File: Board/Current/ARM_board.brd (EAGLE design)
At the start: 101.6 x 81.3 mm, 178 parts, among them IC3 STM32F437VI, IC4 LM358DT, J1 USART/I2C, J10 ANALOG, J11 DGND, J12 DPWR, J13 DIGITAL, J14 SGND, J15 SPWR, J16 SERVO, J2 I2C2/USART3, J3 USART2, J5 SPI, J6 Bluesmirf, J7 SWD, J8 AGND, J9 APWR, Q1 STL4P2UH7, Q2 2STR1230, Q3 STL4P2UH7, SW1 SW, U1 LSM330, U10 BAV99, U11 BAV99, U12 USBLC6-2, U13 USBLC6-2, U14 STMPS2171MTR, U15 MC74HC164, U3 NC7SZU04, U4 L6206Q, U5 L6206Q, U6 SI7617, U7 SI7617, U8 SI7617, U9 SI7617, Y2 8MHz

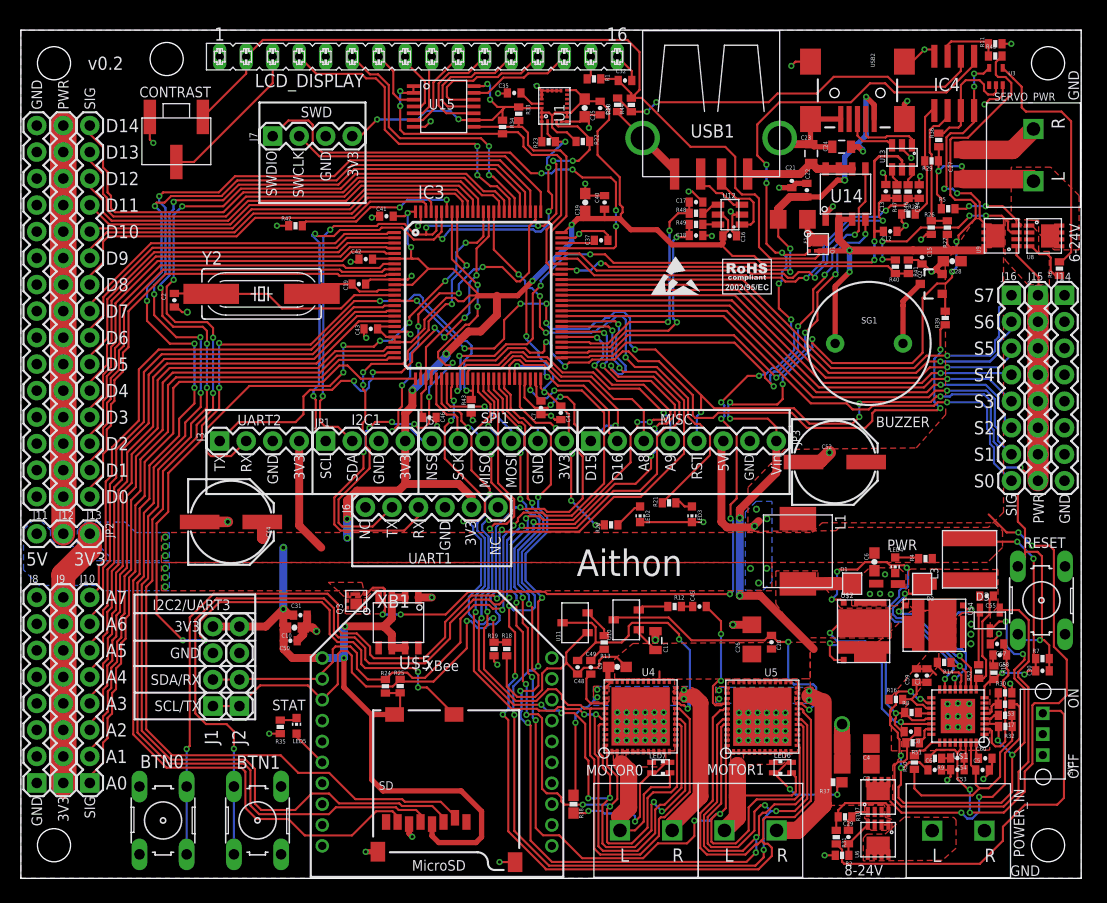
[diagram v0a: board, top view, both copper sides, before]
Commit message: Went through the size of all the passives.
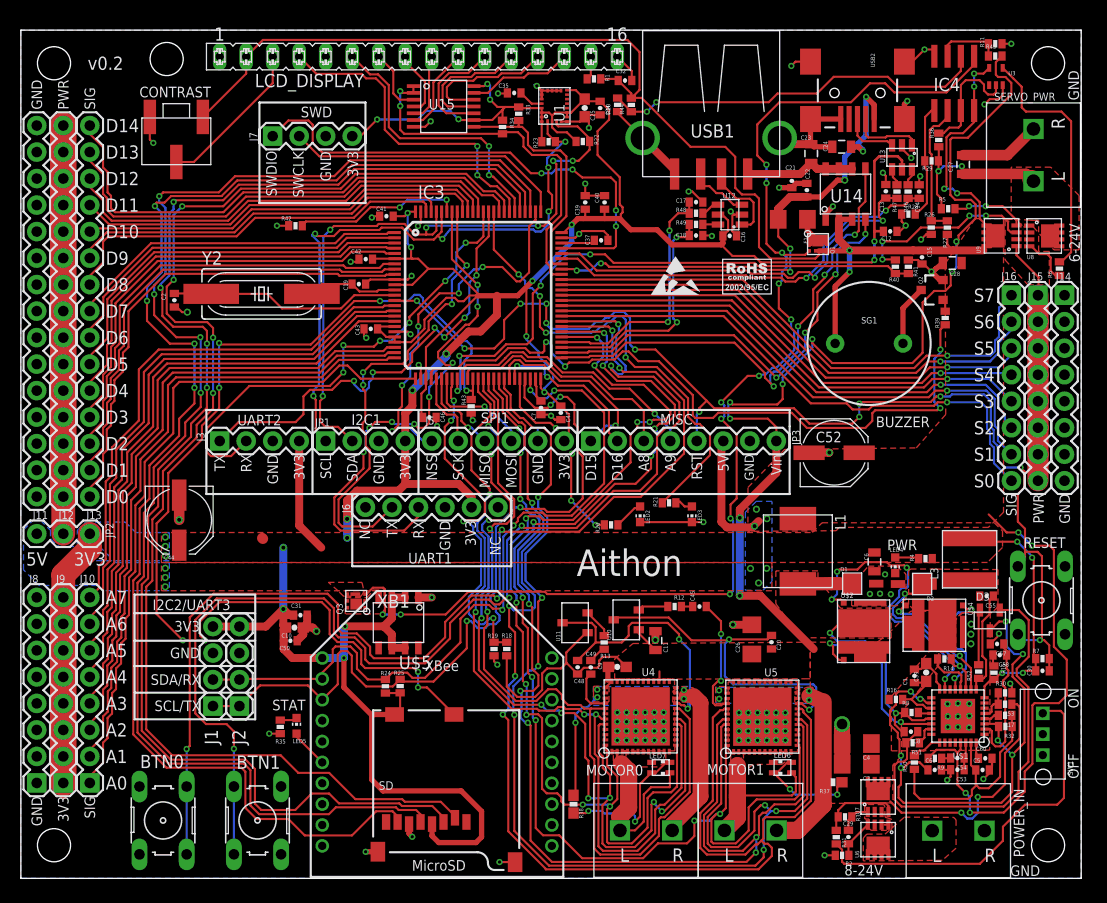
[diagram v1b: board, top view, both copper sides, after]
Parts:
- C27: value 22u -> 33u; device SparkFun:1206 -> SparkFun:0805
- C28, C6: device SparkFun:0603-CAP -> SparkFun:0805
- C39: device SparkFun:0603-CAP -> SparkFun:0402-CAP
- C44, C52: device SparkFun:PANASONIC_E -> SparkFun:PANASONIC_D
- C59: device SparkFun:0402-CAP -> SparkFun:0603-CAP
- moved C44 4.96 mm to (15.2, 34.3), turned to 270 degrees
- moved C1 1.19 mm to (85.6, 19.4)
- moved C59 0.97 mm to (86.7, 19.7)
- moved C52 0.89 mm to (77.9, 40.8)
- moved Q2 0.58 mm to (87.4, 56.4)
- moved R14 0.32 mm to (88.5, 21.0)
- moved C28 0.18 mm to (89.2, 59.0)
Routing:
- net N$39: track 28.5 -> 33.1 mm
- net GND: track 150.6 -> 152.5 mm
- net +3V3: track 373.3 -> 371.9 mm
- net N$15: track 22.1 -> 22.8 mm
- net N$79: track 5.92 -> 6.58 mm
- net ANALOG9: track 26.2 -> 25.7 mm
- net N$28: track 6.39 -> 5.85 mm

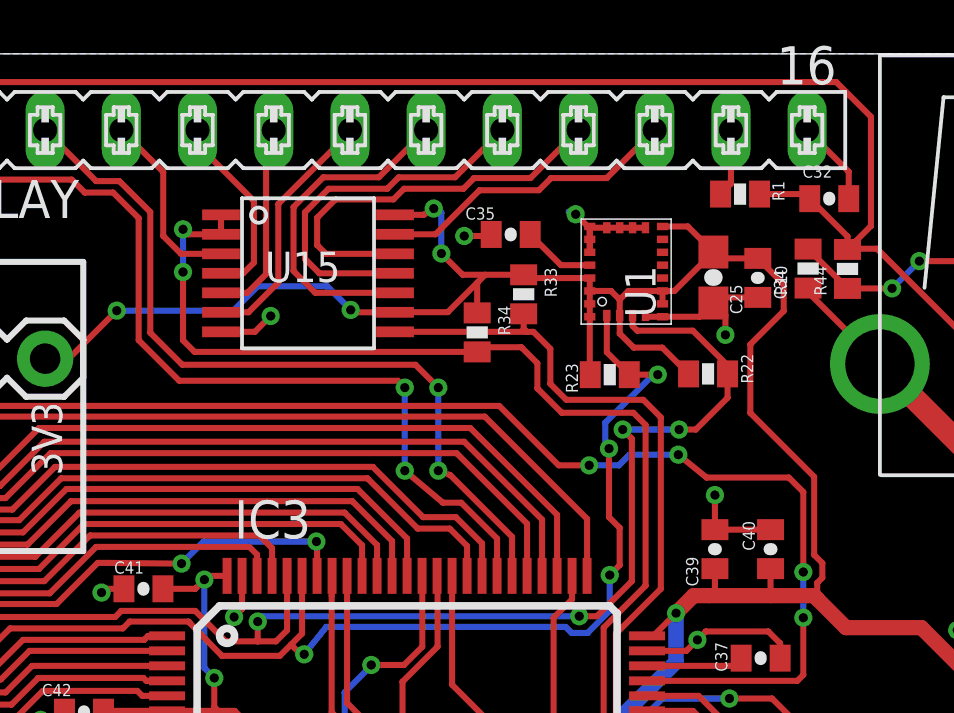
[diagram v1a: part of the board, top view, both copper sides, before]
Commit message: Added more capacitors to the gyro.
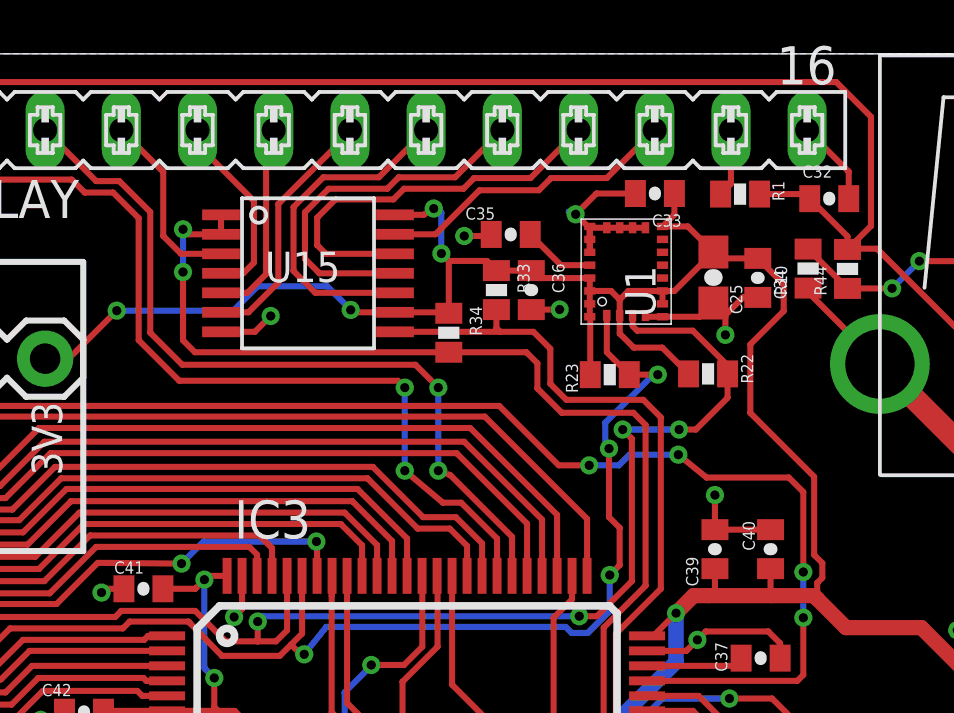
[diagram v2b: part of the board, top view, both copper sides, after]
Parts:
- added C33, C36: 0.1u, SparkFun:0402-CAP
- moved R34 0.95 mm to (45.2, 72.0)
- moved R33 0.92 mm to (46.8, 73.4)
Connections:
- net +3V3: now also C33.1, C36.1
- net GND: now also C33.2, C36.2
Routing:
- net GND: track 152.5 -> 155.8 mm, vias 117 -> 118

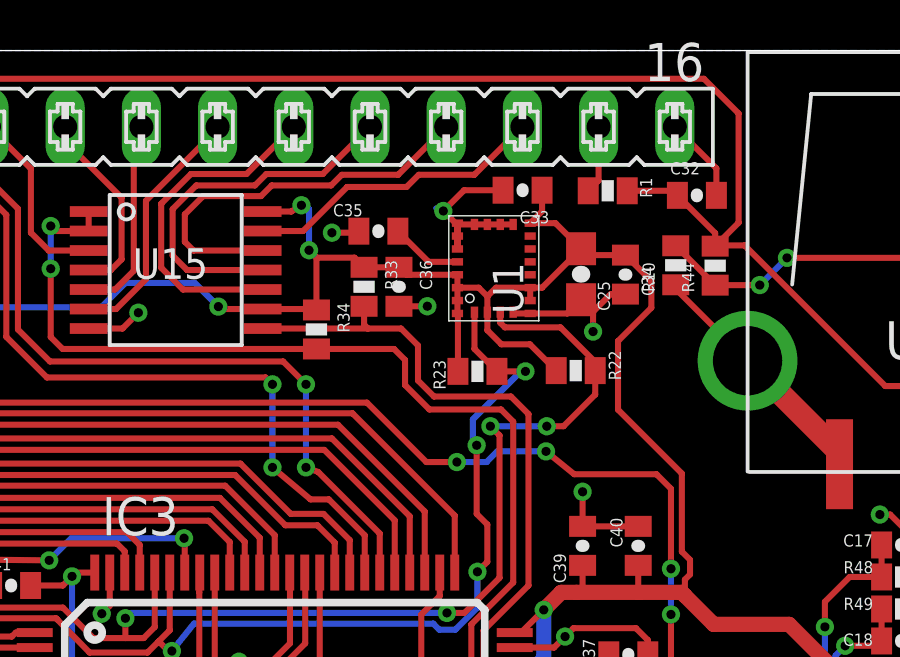
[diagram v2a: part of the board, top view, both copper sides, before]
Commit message: Cleaned up the layout around the gyro a bit.
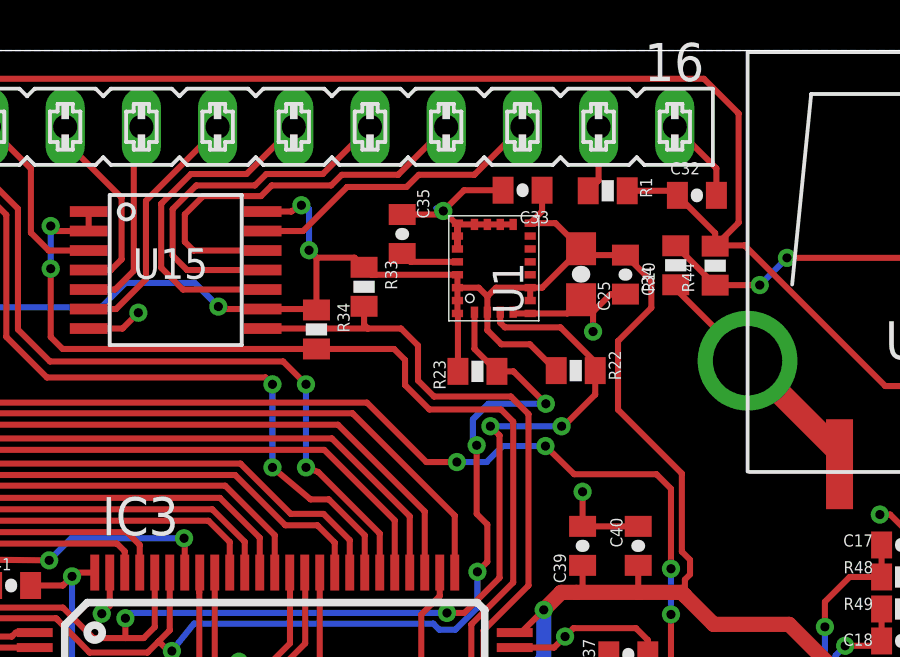
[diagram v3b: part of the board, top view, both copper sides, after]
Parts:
- removed C36: 0.1u, SparkFun:0402-CAP
- moved C35 0.80 mm to (48.1, 75.2), turned to 90 degrees
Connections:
- net +3V3: no longer C36.1
- net GND: no longer C36.2
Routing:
- net I2C1_SCL: track 60.5 -> 61.9 mm
- net GND: track 155.8 -> 155.4 mm, vias 118 -> 116
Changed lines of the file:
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@@
 <attribute name="VALUE" x="56.460390625" y="72.7735375" size="0.4064" layer="27" font="vector" rot="R180"/>
 </element>
-<element name="C35" library="SparkFun" package="0402-CAP" value="10n" x="47.2694" y="75.2602" smashed="yes" rot="R180">
-<attribute name="NAME" x="46.7487" y="76.1619" size="0.4064" layer="25" font="vector" rot="R180"/>
-<attribute name="VALUE" x="48.41748125" y="76.182221875" size="0.4064" layer="27" font="vector" rot="R180"/>
+<element name="C35" library="SparkFun" package="0402-CAP" value="10n" x="48.06315" y="75.16495" smashed="yes" rot="R90">
+<attribute name="NAME" x="48.96485" y="75.68565" size="0.4064" layer="25" font="vector" rot="R90"/>
+<attribute name="VALUE" x="48.985171875" y="74.01686875" size="0.4064" layer="27" font="vector" rot="R90"/>
 </element>
 <element name="F1" library="r_cubed" package="1206" value="1A" x="73.968609375" y="63.14948125" smashed="yes" rot="R180">
@@
 <element name="R53" library="SparkFun" package="0402-RES" value="330k" x="94.30385" y="16.6878" rot="R180"/>
 <element name="C33" library="SparkFun" package="0402-CAP" value="0.1u" x="52.07635" y="76.62545" rot="R180"/>
-<element name="C36" library="SparkFun" package="0402-CAP" value="0.1u" x="47.9552" y="73.406" rot="R270"/>
 </elements>
 <signals>
@@
 <wire x1="87.5284" y1="79.4258" x2="86.586059375" y2="79.423259375" width="0.2032" layer="1"/>
 <via x="86.586059375" y="79.423259375" extent="1-16" drill="0.3048"/>
-<wire x1="46.6194" y1="75.2602" x2="46.4566" y2="75.2094" width="0.2032" layer="1"/>
-<wire x1="46.4566" y1="75.2094" x2="45.72" y2="75.2094" width="0.2032" layer="1"/>
-<via x="45.72" y="75.2094" extent="1-16" drill="0.3048"/>
 <wire x1="37.613" y1="72.0148" x2="38.7408" y2="72.0148" width="0.2032" layer="1"/>
 <wire x1="38.7408" y1="72.0148" x2="39.2684" y2="72.5424" width="0.2032" layer="1"/>
@@
 <contactref element="C33" pad="2"/>
 <contactref element="C34" pad="2"/>
-<contactref element="C36" pad="2"/>
 <wire x1="55.50535" y1="73.1624" x2="55.0132" y2="73.1624" width="0.2032" layer="1"/>
 <wire x1="55.0132" y1="73.1624" x2="54.42585" y2="72.57505" width="0.2032" layer="1"/>
 <wire x1="50.1269" y1="76.62545" x2="49.43475" y2="75.9333" width="0.2032" layer="1"/>
 <wire x1="51.42635" y1="76.62545" x2="50.1269" y2="76.62545" width="0.2032" layer="1"/>
-<wire x1="47.9552" y1="72.756" x2="48.89905" y2="72.756" width="0.2032" layer="1"/>
-<wire x1="48.89905" y1="72.756" x2="48.90135" y2="72.7583" width="0.2032" layer="1"/>
-<via x="48.90135" y="72.7583" extent="1-16" drill="0.3048"/>
+<wire x1="48.06315" y1="75.81495" x2="49.3164" y2="75.81495" width="0.2032" layer="1"/>
+<wire x1="49.3164" y1="75.81495" x2="49.43475" y2="75.9333" width="0.2032" layer="1"/>
 </signal>
 <signal name="5V">
@@
 <wire x1="51.1596" y1="70.9058" x2="51.2214" y2="70.5866" width="0.2032" layer="1"/>
 <wire x1="28.4226" y1="61.5442" x2="28.194" y2="61.7728" width="0.2032" layer="1"/>
-<wire x1="51.2214" y1="70.5866" x2="52.1716" y2="70.5866" width="0.2032" layer="1"/>
-<via x="52.1716" y="70.5866" extent="1-16" drill="0.3048"/>
-<wire x1="52.1716" y1="70.5866" x2="52.0192" y2="70.5866" width="0.2032" layer="16"/>
-<wire x1="52.0192" y1="70.5866" x2="50.419" y2="68.9864" width="0.2032" layer="16"/>
+<via x="52.85105" y="69.5071" extent="1-16" drill="0.3048"/>
 <wire x1="50.419" y1="68.9864" x2="50.419" y2="68.2498" width="0.2032" layer="16"/>
 <wire x1="50.419" y1="68.2498" x2="50.546" y2="68.1228" width="0.2032" layer="16"/>
@@
 <wire x1="50.4725" y1="72.55945" x2="50.4725" y2="71.3355" width="0.2032" layer="1"/>
 <wire x1="50.4725" y1="71.3355" x2="51.2214" y2="70.5866" width="0.2032" layer="1"/>
+<wire x1="52.85105" y1="69.5071" x2="50.9397" y2="69.5071" width="0.2032" layer="16"/>
+<wire x1="50.9397" y1="69.5071" x2="50.419" y2="68.9864" width="0.2032" layer="16"/>
+<wire x1="51.2214" y1="70.5866" x2="51.77155" y2="70.5866" width="0.2032" layer="1"/>
+<wire x1="51.77155" y1="70.5866" x2="52.85105" y2="69.5071" width="0.2032" layer="1"/>
 </signal>
 <signal name="I2C1_SDA">
@@
 <wire x1="51.308" y1="68.453" x2="51.0032" y2="68.7578" width="0.2032" layer="1"/>
 <via x="51.0032" y="68.7578" extent="1-16" drill="0.3048"/>
-<wire x1="51.0032" y1="68.7578" x2="52.8828" y2="68.7578" width="0.2032" layer="16"/>
-<via x="52.8828" y="68.7578" extent="1-16" drill="0.3048"/>
-<wire x1="52.8828" y1="68.7578" x2="53.4416" y2="68.7578" width="0.2032" layer="1"/>
+<wire x1="51.0032" y1="68.7578" x2="53.3781" y2="68.7578" width="0.2032" layer="16"/>
+<via x="53.3781" y="68.7578" extent="1-16" drill="0.3048"/>
+<wire x1="53.3781" y1="68.7578" x2="53.4416" y2="68.7578" width="0.2032" layer="1"/>
 <wire x1="36.7538" y1="62.7126" x2="34.29" y2="62.7126" width="0.2032" layer="1"/>
 <wire x1="34.29" y1="62.7126" x2="34.0868" y2="62.5094" width="0.2032" layer="1"/>
@@
 <wire x1="57.023" y1="66.675" x2="56.5404" y2="67.1576" width="0.2032" layer="1"/>
 <wire x1="56.5404" y1="67.1576" x2="53.7972" y2="67.1576" width="0.2032" layer="1"/>
-<wire x1="53.7972" y1="67.1576" x2="52.8574" y2="67.9196" width="0.2032" layer="1"/>
-<via x="52.8574" y="67.9196" extent="1-16" drill="0.3048"/>
+<wire x1="53.7972" y1="67.1576" x2="52.83835" y2="68.0974" width="0.2032" layer="1"/>
+<via x="52.83835" y="68.0974" extent="1-16" drill="0.3048"/>
 <wire x1="50.8762" y1="67.564" x2="49.8856" y2="67.564" width="0.2032" layer="16"/>
 <via x="49.8856" y="67.564" extent="1-16" drill="0.3048"/>
@@
 <wire x1="27.559" y1="72.6186" x2="25.6286" y2="72.6186" width="0.2032" layer="1"/>
 <wire x1="25.6286" y1="72.6186" x2="24.13" y2="71.12" width="0.2032" layer="1"/>
-<wire x1="52.8574" y1="67.9196" x2="51.2318" y2="67.9196" width="0.2032" layer="16"/>
-<wire x1="51.2318" y1="67.9196" x2="50.8762" y2="67.564" width="0.2032" layer="16"/>
+<wire x1="51.4096" y1="68.0974" x2="50.8762" y2="67.564" width="0.2032" layer="16"/>
 <via x="57.023" y="64.008" extent="1-16" drill="0.3048"/>
 <wire x1="57.023" y1="64.008" x2="57.023" y2="62.484" width="0.2032" layer="16"/>
@@
 <wire x1="57.023" y1="60.579" x2="56.824" y2="60.38" width="0.2032" layer="1"/>
 <wire x1="51.815" y1="60.38" x2="56.824" y2="60.38" width="0.2032" layer="1"/>
+<wire x1="52.83835" y1="68.0974" x2="51.4096" y2="68.0974" width="0.2032" layer="16"/>
 </signal>
 <signal name="SWDCLK">
@@
 <contactref element="U1" pad="13"/>
 <contactref element="C33" pad="1"/>
-<contactref element="C36" pad="1"/>
 <wire x1="49.905" y1="73.37695" x2="49.905" y2="73.80695" width="0.2032" layer="1"/>
 <wire x1="49.905" y1="72.51695" x2="49.905" y2="72.94695" width="0.2032" layer="1"/>
@@
 <wire x1="45.20565" y1="74.37755" x2="46.4716" y2="74.37755" width="0.2032" layer="1"/>
 <wire x1="46.4716" y1="74.37755" x2="46.79315" y2="74.056" width="0.2032" layer="1"/>
-<wire x1="46.79315" y1="74.056" x2="47.9552" y2="74.056" width="0.2032" layer="1"/>
-<wire x1="49.905" y1="73.80695" x2="48.20425" y2="73.80695" width="0.2032" layer="1"/>
-<wire x1="48.20425" y1="73.80695" x2="47.9552" y2="74.056" width="0.2032" layer="1"/>
+<wire x1="49.905" y1="73.80695" x2="47.0422" y2="73.80695" width="0.2032" layer="1"/>
+<wire x1="47.0422" y1="73.80695" x2="46.79315" y2="74.056" width="0.2032" layer="1"/>
 </signal>
 <signal name="N$47">
@@
 <contactref element="C35" pad="1"/>
 <contactref element="U1" pad="21"/>
-<wire x1="49.905" y1="74.23695" x2="48.94265" y2="74.23695" width="0.2032" layer="1"/>
-<wire x1="48.94265" y1="74.23695" x2="47.9194" y2="75.2602" width="0.2032" layer="1"/>
+<wire x1="49.905" y1="74.23695" x2="48.34115" y2="74.23695" width="0.2032" layer="1"/>
+<wire x1="48.34115" y1="74.23695" x2="48.06315" y2="74.51495" width="0.2032" layer="1"/>
 </signal>
 <signal name="N$6">
